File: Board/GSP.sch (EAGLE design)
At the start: 3 parts

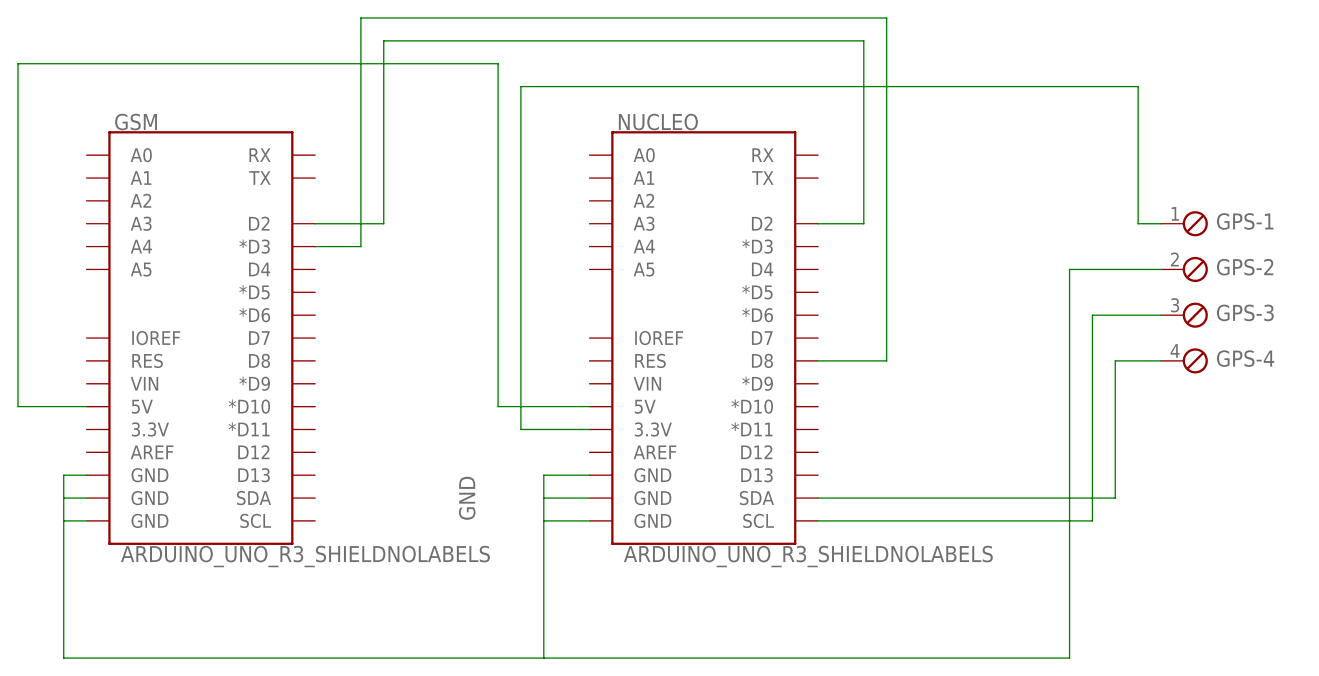
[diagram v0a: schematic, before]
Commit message: Updated board. Test of webpage.
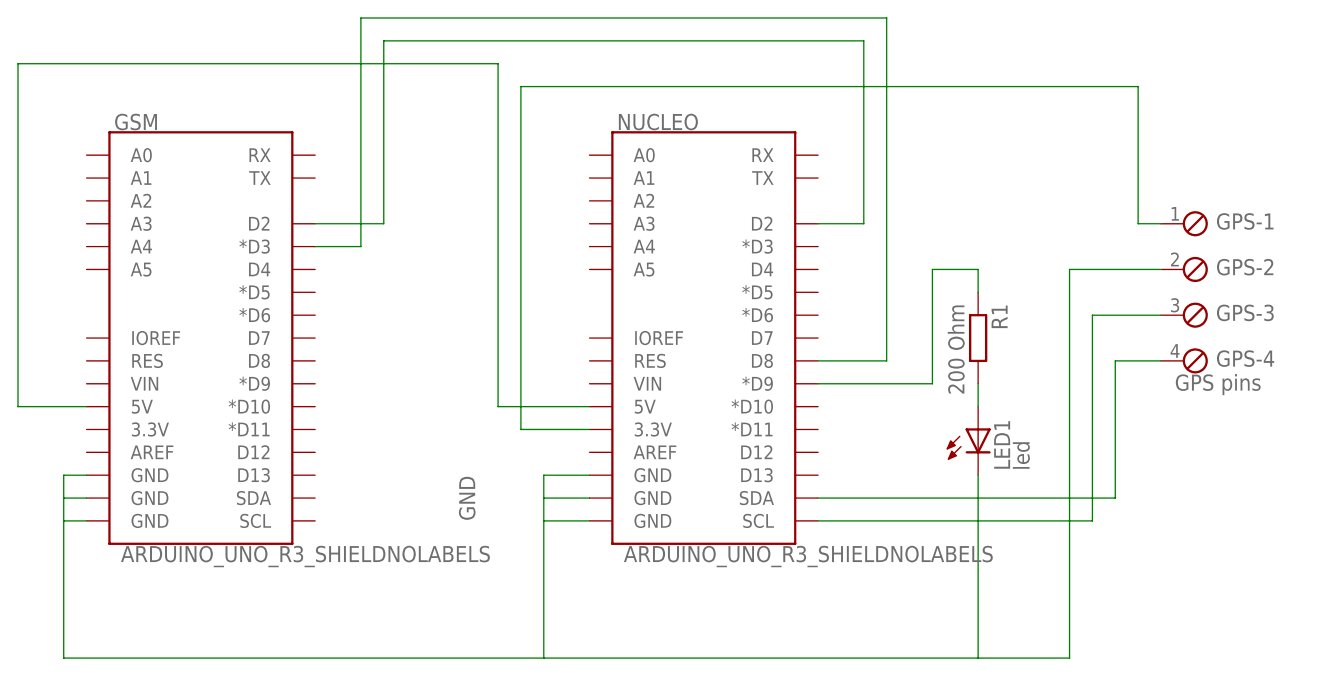
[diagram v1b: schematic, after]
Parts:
- added LED1: led, adafruit:LED3MM
- added R1: 200 Ohm, rcl:R-EU_0204/5
- GPS: value (none) -> GPS pins
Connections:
- new net N$2: NUCLEO.*D9, R1.1
- new net N$3: LED1.A, R1.2
- net GND: now also LED1.C
